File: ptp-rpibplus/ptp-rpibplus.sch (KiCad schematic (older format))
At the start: 3 parts

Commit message: schematic first pass
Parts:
- removed J?: MODULE_HEADER, symbol MODULE_HEADER
- added C?: 10uF, symbol C
- added C?: 100nF, symbol C
- added C?: 1uF, symbol C
- added J?: MODULE_HEADER, symbol MODULE_HEADER
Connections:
- net labels added: 3V3, A_G1/TX, A_G2/RX, A_G3, B_G1/TX, B_G2/RX, B_G3, CLK, GND, MISO, MOSI, SCK, SCL, SDA
- wire segments 0 -> 69
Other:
- moved on the sheet: J?

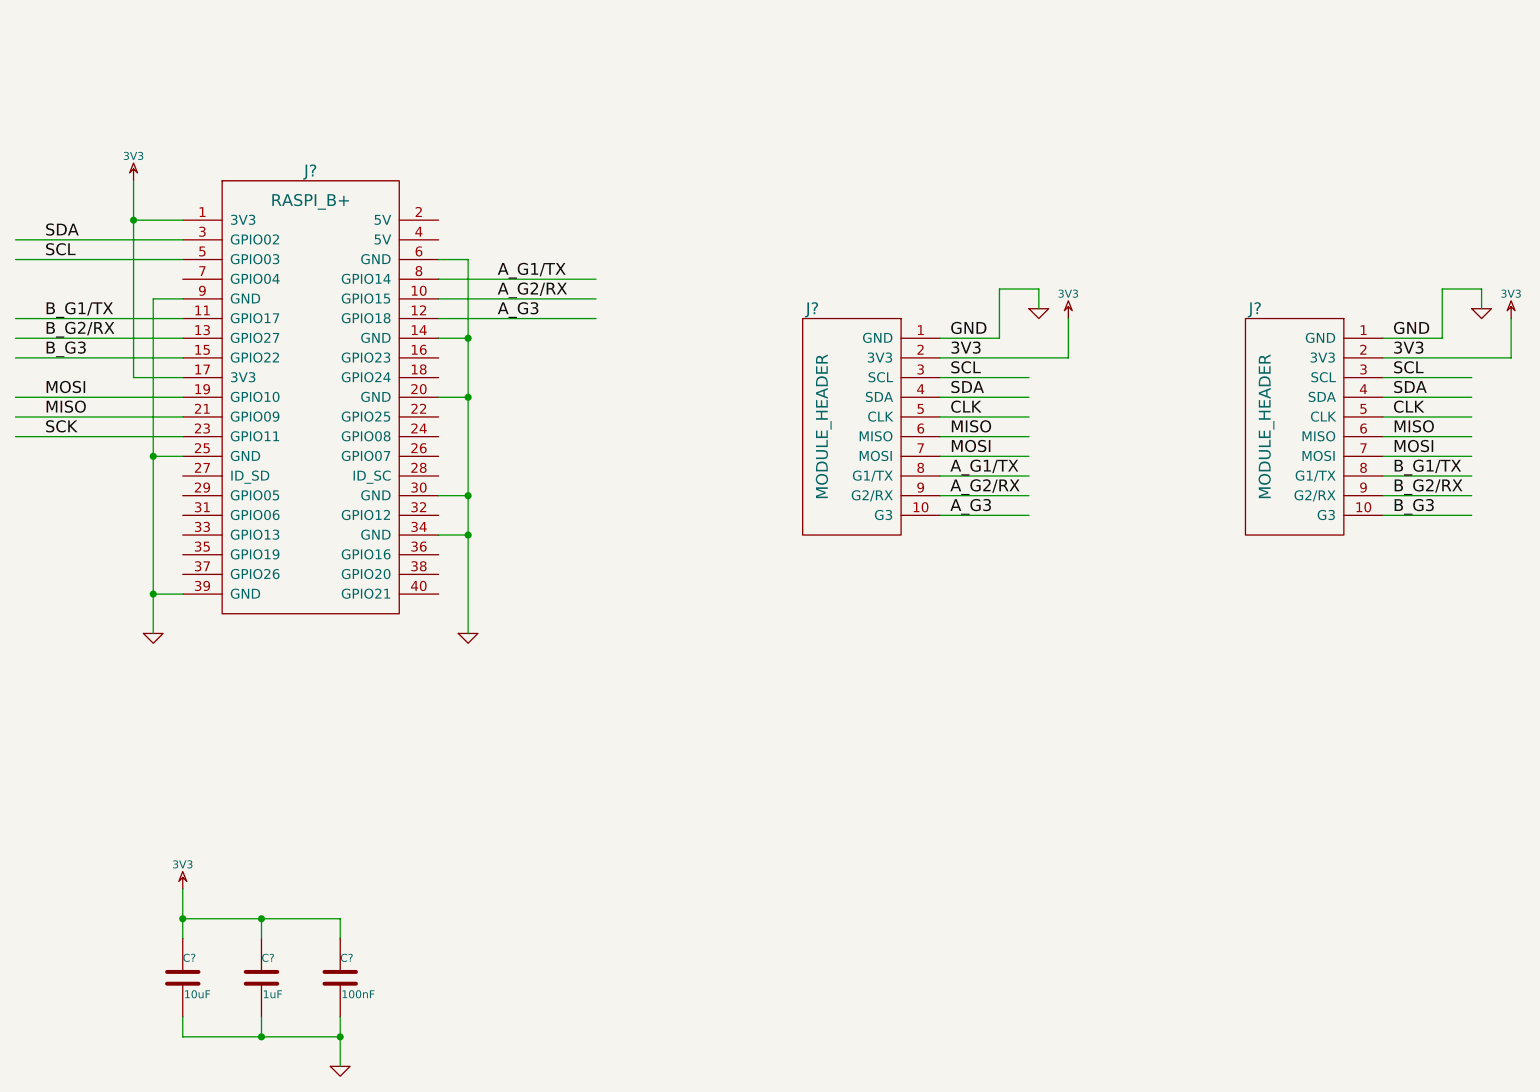
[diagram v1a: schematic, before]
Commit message: netlist, annotation
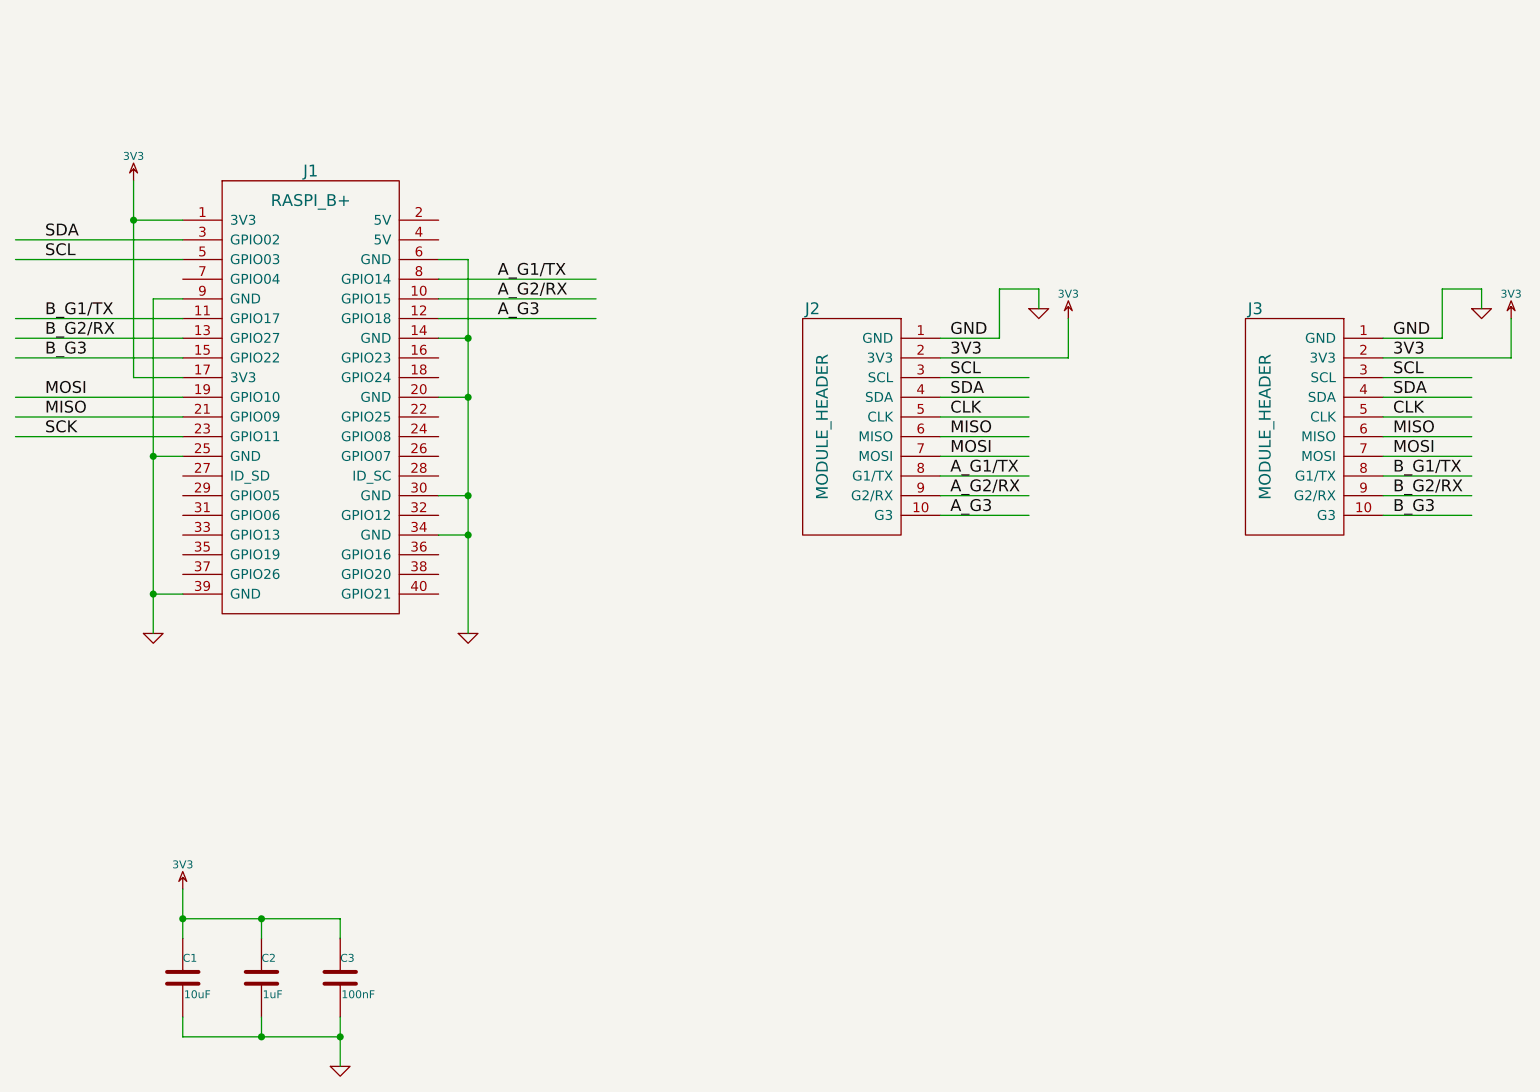
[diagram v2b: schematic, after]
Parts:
- gave numbers to parts that had none: 6
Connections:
- wire segments 69 -> 60
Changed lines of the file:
@@
 $EndDescr
 $Comp
-L RASPI_B+ J?
+L RASPI_B+ J1
 U 1 1 54090FDC
 P 3500 3600
-F 0 "J?" H 3500 4700 60  0000 C CNN
+F 0 "J1" H 3500 4700 60  0000 C CNN
 F 1 "RASPI_B+" H 3500 4550 60  0000 C CNN
 F 2 "" H 3500 4350 60  0000 C CNN
@@
 $EndComp
 $Comp
-L MODULE_HEADER J?
+L MODULE_HEADER J2
 U 1 1 54091105
 P 6400 3750
-F 0 "J?" H 6050 4300 60  0000 C CNN
+F 0 "J2" H 6050 4300 60  0000 C CNN
 F 1 "MODULE_HEADER" V 6100 3700 60  0000 C CNN
 F 2 "" H 6400 3750 60  0000 C CNN
@@
 $EndComp
 $Comp
-L GND #PWR?
+L GND #PWR6
 U 1 1 54090657
 P 7200 3200
-F 0 "#PWR?" H 7200 3200 30  0001 C CNN
+F 0 "#PWR6" H 7200 3200 30  0001 C CNN
 F 1 "GND" H 7200 3130 30  0001 C CNN
 F 2 "" H 7200 3200 60  0000 C CNN
@@
 	7200 3100 7200 3200
 $Comp
-L 3V3 #PWR?
+L 3V3 #PWR7
 U 1 1 540906B9
 P 7350 3250
-F 0 "#PWR?" H 7350 3350 40  0001 C CNN
+F 0 "#PWR7" H 7350 3350 40  0001 C CNN
 F 1 "3V3" H 7350 3375 40  0000 C CNN
 F 2 "" H 7350 3250 60  0000 C CNN
@@
 MOSI
 $Comp
-L MODULE_HEADER J?
+L MODULE_HEADER J3
 U 1 1 54090A08
 P 8650 3750
-F 0 "J?" H 8300 4300 60  0000 C CNN
+F 0 "J3" H 8300 4300 60  0000 C CNN
 F 1 "MODULE_HEADER" V 8350 3700 60  0000 C CNN
 F 2 "" H 8650 3750 60  0000 C CNN
@@
 $EndComp
 $Comp
-L GND #PWR?
+L GND #PWR8
 U 1 1 54090A0E
 P 9450 3200
-F 0 "#PWR?" H 9450 3200 30  0001 C CNN
+F 0 "#PWR8" H 9450 3200 30  0001 C CNN
 F 1 "GND" H 9450 3130 30  0001 C CNN
 F 2 "" H 9450 3200 60  0000 C CNN
@@
 	9450 3100 9450 3200
 $Comp
-L 3V3 #PWR?
+L 3V3 #PWR9
 U 1 1 54090A17
 P 9600 3250
-F 0 "#PWR?" H 9600 3350 40  0001 C CNN
+F 0 "#PWR9" H 9600 3350 40  0001 C CNN
 F 1 "3V3" H 9600 3375 40  0000 C CNN
 F 2 "" H 9600 3250 60  0000 C CNN
@@
 B_G3
 $Comp
-L 3V3 #PWR?
+L 3V3 #PWR1
 U 1 1 54090DA3
 P 2600 2550
-F 0 "#PWR?" H 2600 2650 40  0001 C CNN
+F 0 "#PWR1" H 2600 2650 40  0001 C CNN
 F 1 "3V3" H 2600 2675 40  0000 C CNN
 F 2 "" H 2600 2550 60  0000 C CNN
@@
 $EndComp
 Wire Wire Line
-	2600 2550 2600 2750
-Wire Wire Line
-	2600 2750 2600 3550
+	2600 2550 2600 3550
 Wire Wire Line
 	2600 2750 2850 2750
@@
 Connection ~ 2700 4650
 Wire Wire Line
-	2700 3150 2700 3950
-Wire Wire Line
-	2700 3950 2700 4650
-Wire Wire Line
-	2700 4650 2700 4850
+	2700 3150 2700 4850
 Connection ~ 2700 3950
 Wire Wire Line
-	4300 2950 4300 3350
-Wire Wire Line
-	4300 3350 4300 3650
-Wire Wire Line
-	4300 3650 4300 4150
-Wire Wire Line
-	4300 4150 4300 4350
-Wire Wire Line
-	4300 4350 4300 4850
+	4300 2950 4300 4850
 Connection ~ 4300 3350
 Connection ~ 4300 3650
@@
 Connection ~ 4300 4350
 $Comp
-L GND #PWR?
+L GND #PWR5
 U 1 1 540913D0
 P 4300 4850
-F 0 "#PWR?" H 4300 4850 30  0001 C CNN
+F 0 "#PWR5" H 4300 4850 30  0001 C CNN
 F 1 "GND" H 4300 4780 30  0001 C CNN
 F 2 "" H 4300 4850 60  0000 C CNN
@@
 $EndComp
 $Comp
-L GND #PWR?
+L GND #PWR2
 U 1 1 540913E4
 P 2700 4850
-F 0 "#PWR?" H 2700 4850 30  0001 C CNN
+F 0 "#PWR2" H 2700 4850 30  0001 C CNN
 F 1 "GND" H 2700 4780 30  0001 C CNN
 F 2 "" H 2700 4850 60  0000 C CNN
@@
 $EndComp
 $Comp
-L C C?
+L C C1
 U 1 1 54091A17
 P 2850 6600
-F 0 "C?" H 2850 6700 40  0000 L CNN
+F 0 "C1" H 2850 6700 40  0000 L CNN
 F 1 "10uF" H 2856 6515 40  0000 L CNN
 F 2 "" H 2888 6450 30  0000 C CNN
@@
 $EndComp
 $Comp
-L C C?
+L C C3
 U 1 1 54091CCA
 P 3650 6600
-F 0 "C?" H 3650 6700 40  0000 L CNN
+F 0 "C3" H 3650 6700 40  0000 L CNN
 F 1 "100nF" H 3656 6515 40  0000 L CNN
 F 2 "" H 3688 6450 30  0000 C CNN
@@
 $EndComp
 Wire Wire Line
-	2850 6150 2850 6300
-Wire Wire Line
-	2850 6300 2850 6400
+	2850 6150 2850 6400
 Wire Wire Line
 	2850 6300 3650 6300
@@
 	3650 6300 3650 6400
 Wire Wire Line
-	3650 6800 3650 6900
-Wire Wire Line
-	3650 6900 3650 7050
+	3650 6800 3650 7050
 Wire Wire Line
 	3650 6900 2850 6900
@@
 Connection ~ 2850 6300
 $Comp
-L 3V3 #PWR?
+L 3V3 #PWR3
 U 1 1 5409236C
 P 2850 6150
-F 0 "#PWR?" H 2850 6250 40  0001 C CNN
+F 0 "#PWR3" H 2850 6250 40  0001 C CNN
 F 1 "3V3" H 2850 6275 40  0000 C CNN
 F 2 "" H 2850 6150 60  0000 C CNN
@@
 $EndComp
 $Comp
-L GND #PWR?
+L GND #PWR4
 U 1 1 54092380
 P 3650 7050
-F 0 "#PWR?" H 3650 7050 30  0001 C CNN
+F 0 "#PWR4" H 3650 7050 30  0001 C CNN
 F 1 "GND" H 3650 6980 30  0001 C CNN
 F 2 "" H 3650 7050 60  0000 C CNN
@@
 A_G3
 $Comp
-L C C?
+L C C2
 U 1 1 54093199
 P 3250 6600
-F 0 "C?" H 3250 6700 40  0000 L CNN
+F 0 "C2" H 3250 6700 40  0000 L CNN
 F 1 "1uF" H 3256 6515 40  0000 L CNN
 F 2 "" H 3288 6450 30  0000 C CNN

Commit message: close to refresh
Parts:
- C1: footprint (none) -> Capacitors_SMD:c_0805
- C2, C3: footprint (none) -> Capacitors_SMD:c_0402
- J1: footprint (none) -> Pin_Headers:Pin_Header_Straight_2x20
- J2, J3: footprint (none) -> parts:MODULE_HEADER_TESSEL
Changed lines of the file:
@@
 F 0 "J1" H 3500 4700 60  0000 C CNN
 F 1 "RASPI_B+" H 3500 4550 60  0000 C CNN
-F 2 "" H 3500 4350 60  0000 C CNN
+F 2 "Pin_Headers:Pin_Header_Straight_2x20" H 3500 4350 60  0001 C CNN
 F 3 "" H 3500 4350 60  0000 C CNN
 	1    3500 3600
@@
 F 0 "J2" H 6050 4300 60  0000 C CNN
 F 1 "MODULE_HEADER" V 6100 3700 60  0000 C CNN
-F 2 "" H 6400 3750 60  0000 C CNN
+F 2 "parts:MODULE_HEADER_TESSEL" H 6400 3750 60  0001 C CNN
 F 3 "" H 6400 3750 60  0000 C CNN
 	1    6400 3750
@@
 F 0 "J3" H 8300 4300 60  0000 C CNN
 F 1 "MODULE_HEADER" V 8350 3700 60  0000 C CNN
-F 2 "" H 8650 3750 60  0000 C CNN
+F 2 "parts:MODULE_HEADER_TESSEL" H 8650 3750 60  0001 C CNN
 F 3 "" H 8650 3750 60  0000 C CNN
 	1    8650 3750
@@
 F 0 "C1" H 2850 6700 40  0000 L CNN
 F 1 "10uF" H 2856 6515 40  0000 L CNN
-F 2 "" H 2888 6450 30  0000 C CNN
+F 2 "Capacitors_SMD:c_0805" H 2888 6450 30  0001 C CNN
 F 3 "" H 2850 6600 60  0000 C CNN
 	1    2850 6600
@@
 F 0 "C3" H 3650 6700 40  0000 L CNN
 F 1 "100nF" H 3656 6515 40  0000 L CNN
-F 2 "" H 3688 6450 30  0000 C CNN
+F 2 "Capacitors_SMD:c_0402" H 3688 6450 30  0001 C CNN
 F 3 "" H 3650 6600 60  0000 C CNN
 	1    3650 6600
@@
 F 0 "C2" H 3250 6700 40  0000 L CNN
 F 1 "1uF" H 3256 6515 40  0000 L CNN
-F 2 "" H 3288 6450 30  0000 C CNN
+F 2 "Capacitors_SMD:c_0402" H 3288 6450 30  0001 C CNN
 F 3 "" H 3250 6600 60  0000 C CNN
 	1    3250 6600

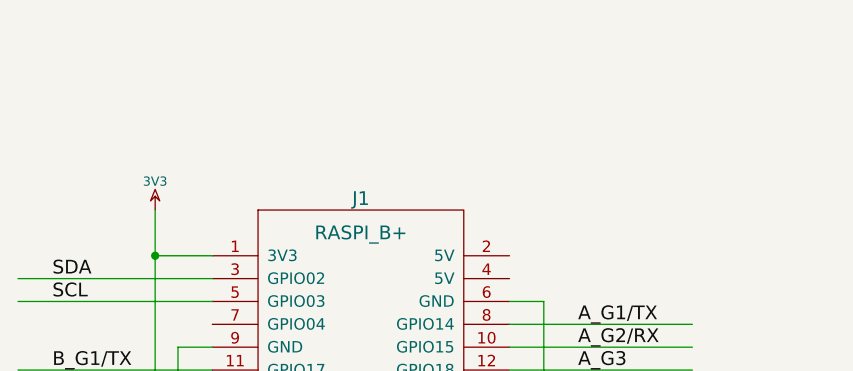
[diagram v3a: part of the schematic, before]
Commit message: note about 3.3 rail, updated silk
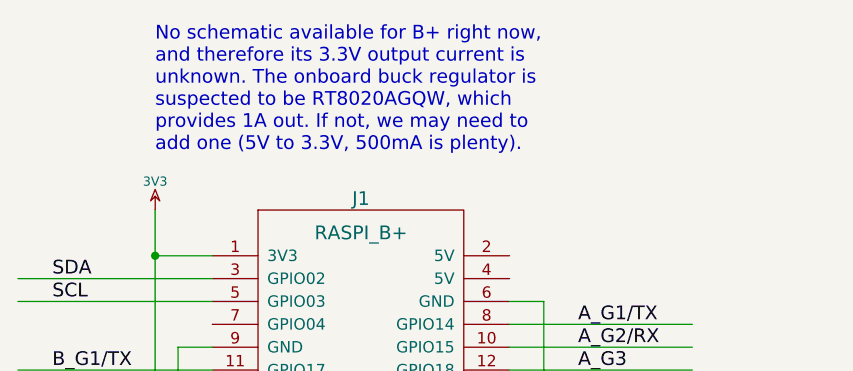
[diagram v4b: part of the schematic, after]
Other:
- note added: "No schematic available for B+ right now, \nand therefore its 3.3V output current is\nunknown. The onboard buck regulator is\nsuspected to be RT8020AGQW, which\nprovides 1A out. If not, we may need to\nadd one (5V to 3.3V, 500mA is plenty)."
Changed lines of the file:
@@
-$EndComp
-$Comp
-L MODULE_HEADER J2
-U 1 1 54091105
-P 6400 3750
-F 0 "J2" H 6050 4300 60  0000 C CNN
-F 1 "MODULE_HEADER" V 6100 3700 60  0000 C CNN
-F 2 "parts:MODULE_HEADER_TESSEL" H 6400 3750 60  0001 C CNN
-F 3 "" H 6400 3750 60  0000 C CNN
-	1    6400 3750
-	1    0    0    -1
 $EndComp
 $Comp
@@
 Text Label 6750 3950 0    60   ~ 0
 MOSI
-$Comp
-L MODULE_HEADER J3
-U 1 1 54090A08
-P 8650 3750
-F 0 "J3" H 8300 4300 60  0000 C CNN
-F 1 "MODULE_HEADER" V 8350 3700 60  0000 C CNN
-F 2 "parts:MODULE_HEADER_TESSEL" H 8650 3750 60  0001 C CNN
-F 3 "" H 8650 3750 60  0000 C CNN
-	1    8650 3750
-	1    0    0    -1
-$EndComp
 $Comp
 L GND #PWR8
@@
 Connection ~ 3250 6300
 Connection ~ 3250 6900
+Text Notes 2600 2300 0    60   ~ 0
+No schematic available for B+ right now, \nand therefore its 3.3V output current is\nunknown. The onboard buck regulator is\nsuspected to be RT8020AGQW, which\nprovides 1A out. If not, we may need to\nadd one (5V to 3.3V, 500mA is plenty).
+$Comp
+L MODULE_HEADER J2
+U 1 1 5409F754
+P 6400 3750
+F 0 "J2" H 6050 4300 60  0000 C CNN
+F 1 "MODULE_HEADER" V 6100 3700 60  0000 C CNN
+F 2 "parts:MODULE_HEADER_TESSEL" H 6400 3750 60  0001 C CNN
+F 3 "" H 6400 3750 60  0000 C CNN
+	1    6400 3750
+	1    0    0    -1
+$EndComp
+$Comp
+L MODULE_HEADER J3
+U 1 1 5409F7C3
+P 8650 3750
+F 0 "J3" H 8300 4300 60  0000 C CNN
+F 1 "MODULE_HEADER" V 8350 3700 60  0000 C CNN
+F 2 "parts:MODULE_HEADER_TESSEL" H 8650 3750 60  0001 C CNN
+F 3 "" H 8650 3750 60  0000 C CNN
+	1    8650 3750
+	1    0    0    -1
+$EndComp
 $EndSCHEMATC

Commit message: ...at least the board has mount holes now
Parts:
- added H1, H2, H3: HOLE, parts:HOLE-2.75mm-6.2mm, symbol HOLE
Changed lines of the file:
@@
 $EndComp
 $Comp
-L GND #PWR6
+L GND #PWR01
 U 1 1 54090657
 P 7200 3200
-F 0 "#PWR6" H 7200 3200 30  0001 C CNN
+F 0 "#PWR01" H 7200 3200 30  0001 C CNN
 F 1 "GND" H 7200 3130 30  0001 C CNN
 F 2 "" H 7200 3200 60  0000 C CNN
@@
 	7200 3100 7200 3200
 $Comp
-L 3V3 #PWR7
+L 3V3 #PWR02
 U 1 1 540906B9
 P 7350 3250
-F 0 "#PWR7" H 7350 3350 40  0001 C CNN
+F 0 "#PWR02" H 7350 3350 40  0001 C CNN
 F 1 "3V3" H 7350 3375 40  0000 C CNN
 F 2 "" H 7350 3250 60  0000 C CNN
@@
 MOSI
 $Comp
-L GND #PWR8
+L GND #PWR03
 U 1 1 54090A0E
 P 9450 3200
-F 0 "#PWR8" H 9450 3200 30  0001 C CNN
+F 0 "#PWR03" H 9450 3200 30  0001 C CNN
 F 1 "GND" H 9450 3130 30  0001 C CNN
 F 2 "" H 9450 3200 60  0000 C CNN
@@
 	9450 3100 9450 3200
 $Comp
-L 3V3 #PWR9
+L 3V3 #PWR04
 U 1 1 54090A17
 P 9600 3250
-F 0 "#PWR9" H 9600 3350 40  0001 C CNN
+F 0 "#PWR04" H 9600 3350 40  0001 C CNN
 F 1 "3V3" H 9600 3375 40  0000 C CNN
 F 2 "" H 9600 3250 60  0000 C CNN
@@
 B_G3
 $Comp
-L 3V3 #PWR1
+L 3V3 #PWR05
 U 1 1 54090DA3
 P 2600 2550
-F 0 "#PWR1" H 2600 2650 40  0001 C CNN
+F 0 "#PWR05" H 2600 2650 40  0001 C CNN
 F 1 "3V3" H 2600 2675 40  0000 C CNN
 F 2 "" H 2600 2550 60  0000 C CNN
@@
 Connection ~ 4300 4350
 $Comp
-L GND #PWR5
+L GND #PWR06
 U 1 1 540913D0
 P 4300 4850
-F 0 "#PWR5" H 4300 4850 30  0001 C CNN
+F 0 "#PWR06" H 4300 4850 30  0001 C CNN
 F 1 "GND" H 4300 4780 30  0001 C CNN
 F 2 "" H 4300 4850 60  0000 C CNN
@@
 $EndComp
 $Comp
-L GND #PWR2
+L GND #PWR07
 U 1 1 540913E4
 P 2700 4850
-F 0 "#PWR2" H 2700 4850 30  0001 C CNN
+F 0 "#PWR07" H 2700 4850 30  0001 C CNN
 F 1 "GND" H 2700 4780 30  0001 C CNN
 F 2 "" H 2700 4850 60  0000 C CNN
@@
 	3650 6800 3650 7050
 Wire Wire Line
-	3650 6900 2850 6900
+	2850 6900 3650 6900
 Wire Wire Line
 	2850 6900 2850 6800
@@
 Connection ~ 2850 6300
 $Comp
-L 3V3 #PWR3
+L 3V3 #PWR08
 U 1 1 5409236C
 P 2850 6150
-F 0 "#PWR3" H 2850 6250 40  0001 C CNN
+F 0 "#PWR08" H 2850 6250 40  0001 C CNN
 F 1 "3V3" H 2850 6275 40  0000 C CNN
 F 2 "" H 2850 6150 60  0000 C CNN
@@
 $EndComp
 $Comp
-L GND #PWR4
+L GND #PWR09
 U 1 1 54092380
 P 3650 7050
-F 0 "#PWR4" H 3650 7050 30  0001 C CNN
+F 0 "#PWR09" H 3650 7050 30  0001 C CNN
 F 1 "GND" H 3650 6980 30  0001 C CNN
 F 2 "" H 3650 7050 60  0000 C CNN
@@
 	1    0    0    -1
 $EndComp
+$Comp
+L HOLE H1
+U 1 1 5409FB3F
+P 5000 6650
+F 0 "H1" H 5000 6800 60  0000 C CNN
+F 1 "HOLE" H 5000 6500 60  0000 C CNN
+F 2 "parts:HOLE-2.75mm-6.2mm" H 5000 6650 60  0001 C CNN
+F 3 "" H 5000 6650 60  0000 C CNN
+	1    5000 6650
+	1    0    0    -1
+$EndComp
+$Comp
+L HOLE H3
+U 1 1 5409FB58
+P 5800 6650
+F 0 "H3" H 5800 6800 60  0000 C CNN
+F 1 "HOLE" H 5800 6500 60  0000 C CNN
+F 2 "parts:HOLE-2.75mm-6.2mm" H 5800 6650 60  0001 C CNN
+F 3 "" H 5800 6650 60  0000 C CNN
+	1    5800 6650
+	1    0    0    -1
+$EndComp
+$Comp
+L HOLE H2
+U 1 1 5409FC68
+P 5400 6650
+F 0 "H2" H 5400 6800 60  0000 C CNN
+F 1 "HOLE" H 5400 6500 60  0000 C CNN
+F 2 "parts:HOLE-2.75mm-6.2mm" H 5400 6650 60  0001 C CNN
+F 3 "" H 5400 6650 60  0000 C CNN
+	1    5400 6650
+	1    0    0    -1
+$EndComp

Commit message: mostly happy. power and ground left.
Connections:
- net labels removed: CLK
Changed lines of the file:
@@
 SDA
 Text Label 6750 3750 0    60   ~ 0
-CLK
+SCK
 Text Label 6750 3850 0    60   ~ 0
 MISO
@@
 SDA
 Text Label 9000 3750 0    60   ~ 0
-CLK
+SCK
 Text Label 9000 3850 0    60   ~ 0
 MISO

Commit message: added ptp rpib+ logo, board dimensions, updated gerbers
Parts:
- added SILK1: logo, parts:PTP-RPI-LOGO, symbol logo
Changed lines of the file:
@@
+	1    0    0    -1
+$EndComp
+$Comp
+L logo SILK1
+U 1 1 540E032E
+P 6200 6650
+F 0 "SILK1" H 6200 6700 60  0000 C CNN
+F 1 "logo" H 6200 6600 60  0000 C CNN
+F 2 "parts:PTP-RPI-LOGO" H 6200 6650 60  0001 C CNN
+F 3 "" H 6200 6650 60  0000 C CNN
+	1    6200 6650
 	1    0    0    -1
 $EndComp
